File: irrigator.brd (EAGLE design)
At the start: 79.7 x 47 mm, 27 parts, among them IC1 MEGA8-AI, IC2 78L05Z, T1 BT136, X1 MSTBA2

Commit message: fix. errors and manual routing
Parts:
- C3: device rcl:C102-054X133 -> rcl:C1206
- moved L1 55.6 mm to (12.6, 18.4), turned to 180 degrees
- moved C3 54.1 mm to (57.5, 33.6), turned to 180 degrees
- moved R8 50.1 mm to (51.2, 29.4), turned to 270 degrees
- moved R7 48.7 mm to (52.0, 33.6), turned to 180 degrees
- moved C4 46.3 mm to (5.70, 20.9)
- moved C1 46.0 mm to (11.2, 36.2), turned to 180 degrees
- moved JP3 44.6 mm to (5.35, 8.22), turned to 270 degrees
- moved T1 41.4 mm to (59.6, 15.6), turned to 270 degrees
- moved LED1 36.5 mm to (35.8, 20.6)
- moved C2 35.3 mm to (20.7, 37.7)
- moved IC1 33.4 mm to (21.6, 22.4)
- moved LED2 31.6 mm to (35.7, 12.6)
- moved IC2 30.2 mm to (17.6, 32.2), turned to 180 degrees
- moved R5 28.1 mm to (46.0, 12.9), turned to 180 degrees
- moved S2 27.5 mm to (30.4, 4.97), turned to 180 degrees
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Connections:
- new net MISO: IC1.16, JP3.1
- new net MOSI: IC1.15, JP3.4
- new net SCK: IC1.17, JP3.3
- net BUTTON_1: now also IC1.13; no longer IC1.12
- net BUTTON_2: now also IC1.12; no longer IC1.13
- net LED_1: now also IC1.9; no longer IC1.15, JP3.4
- net LED_2: now also IC1.10; no longer IC1.16, JP3.1
- net SENS_IN: no longer JP3.3
- net SW: now also IC1.1; no longer IC1.14
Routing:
- net GND: track 0.00 -> 172.2 mm
- net VCC: track 0.00 -> 94.3 mm, vias 0 -> 2
- net RESET: track 0.00 -> 46.2 mm, vias 0 -> 2
- net N$7: track 0.00 -> 44.4 mm
- net N$8: track 0.00 -> 26.8 mm
- net SCK: track 0.00 -> 25.7 mm
- net BUTTON_2: track 0.00 -> 22.7 mm
- net MOSI: track 0.00 -> 20.7 mm
- net N$6: track 0.00 -> 20.4 mm
- net BUTTON_1: track 0.00 -> 20.4 mm
- net MISO: track 0.00 -> 19.3 mm
- net VIN: track 0.00 -> 15.4 mm
- net SENS_IN: track 0.00 -> 13.4 mm
- net LED_2: track 0.00 -> 13.2 mm
- net N$1: track 0.00 -> 12.8 mm
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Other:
- board size 79.7 x 47 mm -> 74.9 x 42.2 mm

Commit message: minor fix.
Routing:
- net N$8: track 26.8 -> 26.3 mm
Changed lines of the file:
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@@
 <wire x1="58.9" y1="33.6" x2="62.66" y2="34" width="0.4064" layer="16"/>
 <wire x1="62.66" y1="34" x2="64.26" y2="33.88" width="0.4064" layer="16"/>
-<wire x1="53.25" y1="18.14" x2="57.45" y2="18.75" width="0.4064" layer="16"/>
-<wire x1="57.45" y1="18.75" x2="63.8" y2="27.3" width="1.6764" layer="16"/>
 <wire x1="63.8" y1="27.3" x2="64.3" y2="33.84" width="1.6764" layer="16"/>
-<wire x1="64.3" y1="33.84" x2="64.26" y2="33.88" width="0" layer="19" extent="1-16"/>
+<wire x1="53.25" y1="18.14" x2="54.64" y2="18.14" width="1.6764" layer="16"/>
+<wire x1="54.64" y1="18.14" x2="63.8" y2="27.3" width="1.6764" layer="16"/>
+<wire x1="64.3" y1="33.84" x2="64.26" y2="33.88" width="0" layer="19" extent="16-16"/>
 </signal>
 <signal name="N$9">

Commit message: board fix
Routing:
- net VCC: track 94.3 -> 128.0 mm
- net RESET: track 46.2 -> 48.4 mm
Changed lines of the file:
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@@
 <wire x1="25.1" y1="31.7" x2="23.498" y2="33.302" width="0.4064" layer="16"/>
 <wire x1="23.498" y1="33.302" x2="23.36" y2="33.302" width="0.4064" layer="16"/>
-<wire x1="19.46" y1="10.008" x2="19.62" y2="9.848" width="0.4064" layer="16"/>
-<wire x1="19.62" y1="9.848" x2="25.1" y2="9.848" width="0.4064" layer="16"/>
-<wire x1="9.1" y1="18.5" x2="11" y2="18.5" width="0.4064" layer="16"/>
-<wire x1="11" y1="18.5" x2="11.1" y2="18.4" width="0.4064" layer="16"/>
-<wire x1="6.62" y1="10.76" x2="6.56" y2="10.76" width="0.4064" layer="16"/>
-<wire x1="6.56" y1="10.76" x2="5.4" y2="9.6" width="0.4064" layer="16"/>
-<wire x1="5.4" y1="9.6" x2="5.4" y2="7" width="0.4064" layer="16"/>
-<wire x1="5.4" y1="7" x2="10.5" y2="7" width="0.4064" layer="16"/>
-<wire x1="10.5" y1="7" x2="12.7" y2="4.8" width="0.4064" layer="16"/>
-<wire x1="12.7" y1="4.8" x2="24.6" y2="4.8" width="0.4064" layer="16"/>
-<wire x1="24.6" y1="4.8" x2="24.6" y2="9.348" width="0.4064" layer="16"/>
-<wire x1="24.6" y1="9.348" x2="25.1" y2="9.848" width="0.4064" layer="16"/>
-<wire x1="8.8" y1="16.8" x2="8.8" y2="17.6" width="0.4064" layer="16"/>
-<wire x1="8.8" y1="17.6" x2="9.1" y2="18.5" width="0.4064" layer="16"/>
-<via x="8.8" y="16.8" extent="1-16" drill="0.8" diameter="1.6764"/>
-<wire x1="8.8" y1="16.8" x2="9" y2="13.8" width="0.4064" layer="1"/>
-<wire x1="9" y1="13.8" x2="9.2" y2="10.9" width="0.4064" layer="1"/>
-<via x="9.2" y="10.9" extent="1-16" drill="0.8" diameter="1.6764"/>
-<wire x1="9.2" y1="10.9" x2="6.76" y2="10.9" width="0.4064" layer="16"/>
-<wire x1="6.76" y1="10.9" x2="6.62" y2="10.76" width="0.4064" layer="16"/>
 <wire x1="25.8926" y1="21.2" x2="27.1" y2="21.2" width="0.4064" layer="16"/>
 <wire x1="27.1" y1="21.2" x2="27.7" y2="21.8" width="0.4064" layer="16"/>
 <wire x1="27.7" y1="21.8" x2="27.7" y2="22.720471875" width="0.4064" layer="16"/>
 <wire x1="27.7" y1="22.720471875" x2="27.59071875" y2="22.829753125" width="0.4064" layer="16"/>
-<wire x1="11" y1="18.5" x2="11.048" y2="25.04" width="0" layer="19" extent="16-16"/>
+<wire x1="6.62" y1="10.76" x2="6.56" y2="10.76" width="0.4064" layer="16"/>
+<wire x1="6.56" y1="10.76" x2="5.3" y2="9.5" width="0.4064" layer="16"/>
+<wire x1="5.3" y1="9.5" x2="5.3" y2="7.2" width="0.4064" layer="16"/>
+<wire x1="5.3" y1="7.2" x2="5.5" y2="7" width="0.4064" layer="16"/>
+<wire x1="5.5" y1="7" x2="7.8" y2="7" width="0.4064" layer="16"/>
+<wire x1="7.8" y1="7" x2="9.9" y2="4.9" width="0.4064" layer="16"/>
+<wire x1="9.9" y1="4.9" x2="25.2" y2="4.9" width="0.4064" layer="16"/>
+<wire x1="25.2" y1="4.9" x2="35" y2="4.9" width="0.4064" layer="16"/>
+<wire x1="35" y1="4.9" x2="35.7" y2="5.9" width="0.4064" layer="16"/>
+<wire x1="35.7" y1="5.9" x2="35.7" y2="21.5" width="0.4064" layer="16"/>
+<wire x1="35.7" y1="21.5" x2="35" y2="22.9" width="0.4064" layer="16"/>
+<wire x1="35" y1="22.9" x2="31.6" y2="22.9" width="0.4064" layer="16"/>
+<wire x1="25.1" y1="9.848" x2="25.1" y2="5" width="0.4064" layer="16"/>
+<wire x1="25.1" y1="5" x2="25.2" y2="4.9" width="0.4064" layer="16"/>
+<wire x1="25.1" y1="9.848" x2="19.62" y2="9.848" width="0.4064" layer="16"/>
+<wire x1="19.62" y1="9.848" x2="19.46" y2="10.008" width="0.4064" layer="16"/>
+<wire x1="11.1" y1="18.4" x2="8.8" y2="18.4" width="0.4064" layer="16"/>
+<wire x1="8.8" y1="18.4" x2="8.3" y2="17.9" width="0.4064" layer="16"/>
+<via x="8.3" y="17.9" extent="1-16" drill="0.8" diameter="1.6764"/>
+<wire x1="8.3" y1="17.9" x2="8.3" y2="11.7" width="0.4064" layer="1"/>
+<wire x1="8.3" y1="11.7" x2="9.8" y2="10.9" width="0.4064" layer="1"/>
+<via x="9.8" y="10.9" extent="1-16" drill="0.8" diameter="1.6764"/>
+<wire x1="9.8" y1="10.9" x2="6.76" y2="10.9" width="0.4064" layer="16"/>
+<wire x1="6.76" y1="10.9" x2="6.62" y2="10.76" width="0.4064" layer="16"/>
 </signal>
 <signal name="BUTTON_2">
@@
 <wire x1="4.08" y1="4.92" x2="6.5" y2="3" width="0.4064" layer="16"/>
 <via x="6.5" y="3" extent="1-16" drill="0.8" diameter="1.6764"/>
-<wire x1="6.5" y1="3" x2="12.6" y2="10.3" width="0.4064" layer="1"/>
-<wire x1="12.6" y1="10.3" x2="20.1" y2="28.7" width="0.4064" layer="1"/>
 <via x="20.1" y="28.7" extent="1-16" drill="0.8" diameter="1.6764"/>
 <wire x1="20.1" y1="28.7" x2="21.7" y2="28.7" width="0.4064" layer="16"/>
 <wire x1="21.7" y1="28.7" x2="22" y2="28.4" width="0.4064" layer="16"/>
+<wire x1="6.5" y1="3" x2="12.8" y2="7.3" width="0.4064" layer="1"/>
+<wire x1="12.8" y1="7.3" x2="12.8" y2="19.4" width="0.4064" layer="1"/>
+<wire x1="12.8" y1="19.4" x2="20.1" y2="28.7" width="0.4064" layer="1"/>
 </signal>
 <signal name="LED_1">

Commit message: brd fix.
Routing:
- net VCC: track 128.0 -> 129.3 mm
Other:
- board size 74.9 x 42.2 mm -> 74.9 x 42.4 mm
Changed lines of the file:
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@@
 <layer number="27" name="tValues" color="7" fill="1" visible="yes" active="yes"/>
 <layer number="28" name="bValues" color="7" fill="1" visible="yes" active="yes"/>
-<layer number="29" name="tStop" color="7" fill="3" visible="no" active="yes"/>
-<layer number="30" name="bStop" color="7" fill="6" visible="no" active="yes"/>
-<layer number="31" name="tCream" color="7" fill="4" visible="no" active="yes"/>
-<layer number="32" name="bCream" color="7" fill="5" visible="no" active="yes"/>
-<layer number="33" name="tFinish" color="6" fill="3" visible="no" active="yes"/>
-<layer number="34" name="bFinish" color="6" fill="6" visible="no" active="yes"/>
-<layer number="35" name="tGlue" color="7" fill="4" visible="no" active="yes"/>
-<layer number="36" name="bGlue" color="7" fill="5" visible="no" active="yes"/>
-<layer number="37" name="tTest" color="7" fill="1" visible="no" active="yes"/>
-<layer number="38" name="bTest" color="7" fill="1" visible="no" active="yes"/>
+<layer number="29" name="tStop" color="7" fill="3" visible="yes" active="yes"/>
+<layer number="30" name="bStop" color="7" fill="6" visible="yes" active="yes"/>
+<layer number="31" name="tCream" color="7" fill="4" visible="yes" active="yes"/>
+<layer number="32" name="bCream" color="7" fill="5" visible="yes" active="yes"/>
+<layer number="33" name="tFinish" color="6" fill="3" visible="yes" active="yes"/>
+<layer number="34" name="bFinish" color="6" fill="6" visible="yes" active="yes"/>
+<layer number="35" name="tGlue" color="7" fill="4" visible="yes" active="yes"/>
+<layer number="36" name="bGlue" color="7" fill="5" visible="yes" active="yes"/>
+<layer number="37" name="tTest" color="7" fill="1" visible="yes" active="yes"/>
+<layer number="38" name="bTest" color="7" fill="1" visible="yes" active="yes"/>
 <layer number="39" name="tKeepout" color="4" fill="11" visible="yes" active="yes"/>
 <layer number="40" name="bKeepout" color="1" fill="11" visible="yes" active="yes"/>
@@
 <layer number="42" name="bRestrict" color="1" fill="10" visible="yes" active="yes"/>
 <layer number="43" name="vRestrict" color="2" fill="10" visible="yes" active="yes"/>
-<layer number="44" name="Drills" color="7" fill="1" visible="no" active="yes"/>
-<layer number="45" name="Holes" color="7" fill="1" visible="no" active="yes"/>
-<layer number="46" name="Milling" color="3" fill="1" visible="no" active="yes"/>
-<layer number="47" name="Measures" color="7" fill="1" visible="no" active="yes"/>
+<layer number="44" name="Drills" color="7" fill="1" visible="yes" active="yes"/>
+<layer number="45" name="Holes" color="7" fill="1" visible="yes" active="yes"/>
+<layer number="46" name="Milling" color="3" fill="1" visible="yes" active="yes"/>
+<layer number="47" name="Measures" color="7" fill="1" visible="yes" active="yes"/>
 <layer number="48" name="Document" color="7" fill="1" visible="yes" active="yes"/>
 <layer number="49" name="Reference" color="7" fill="1" visible="yes" active="yes"/>
@@
 <plain>
 <wire x1="0" y1="0" x2="74.88" y2="0.1" width="0" layer="20"/>
-<wire x1="74.88" y1="0.1" x2="74.78" y2="42.18" width="0" layer="20"/>
-<wire x1="74.78" y1="42.18" x2="0" y2="42.18" width="0" layer="20"/>
+<wire x1="74.88" y1="0.1" x2="74.88" y2="42.38" width="0" layer="20"/>
+<wire x1="74.88" y1="42.38" x2="0" y2="42.18" width="0" layer="20"/>
 <wire x1="0" y1="42.18" x2="0" y2="0" width="0" layer="20"/>
 </plain>
@@
 <wire x1="9.9" y1="4.9" x2="25.2" y2="4.9" width="0.4064" layer="16"/>
 <wire x1="25.2" y1="4.9" x2="35" y2="4.9" width="0.4064" layer="16"/>
-<wire x1="35" y1="4.9" x2="35.7" y2="5.9" width="0.4064" layer="16"/>
-<wire x1="35.7" y1="5.9" x2="35.7" y2="21.5" width="0.4064" layer="16"/>
-<wire x1="35.7" y1="21.5" x2="35" y2="22.9" width="0.4064" layer="16"/>
-<wire x1="35" y1="22.9" x2="31.6" y2="22.9" width="0.4064" layer="16"/>
+<wire x1="35.8" y1="21.5" x2="35.1" y2="22.9" width="0.4064" layer="16"/>
+<wire x1="35.1" y1="22.9" x2="31.6" y2="22.9" width="0.4064" layer="16"/>
 <wire x1="25.1" y1="9.848" x2="25.1" y2="5" width="0.4064" layer="16"/>
 <wire x1="25.1" y1="5" x2="25.2" y2="4.9" width="0.4064" layer="16"/>
@@
 <wire x1="9.8" y1="10.9" x2="6.76" y2="10.9" width="0.4064" layer="16"/>
 <wire x1="6.76" y1="10.9" x2="6.62" y2="10.76" width="0.4064" layer="16"/>
+<wire x1="35.8" y1="21.6" x2="35.8" y2="21.5" width="0.4064" layer="16"/>
+<wire x1="35.8" y1="21.5" x2="35.8" y2="9.2" width="0.4064" layer="16"/>
+<wire x1="35.8" y1="9.2" x2="37.1" y2="7.6" width="0.4064" layer="16"/>
+<wire x1="37.1" y1="7.6" x2="37.1" y2="7" width="0.4064" layer="16"/>
+<wire x1="37.1" y1="7" x2="35" y2="4.9" width="0.4064" layer="16"/>
 </signal>
 <signal name="BUTTON_2">
@@
 <contactref element="OK1" pad="1"/>
 <wire x1="33.022" y1="25.4" x2="35.3" y2="25.4" width="0.4064" layer="16"/>
-<wire x1="35.3" y1="25.4" x2="36.5" y2="26.6" width="0.4064" layer="16"/>
-<wire x1="36.5" y1="26.6" x2="36.5" y2="32.1" width="0.4064" layer="16"/>
-<wire x1="36.5" y1="32.1" x2="38.04" y2="33.64" width="0.4064" layer="16"/>
+<wire x1="35.3" y1="25.4" x2="36.4" y2="26.6" width="0.4064" layer="16"/>
+<wire x1="36.4" y1="26.6" x2="36.4" y2="32.1" width="0.4064" layer="16"/>
+<wire x1="36.4" y1="32.1" x2="38.04" y2="33.64" width="0.4064" layer="16"/>
 <wire x1="38.04" y1="33.64" x2="39.19" y2="33.64" width="0.4064" layer="16"/>
 </signal>

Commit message: fix. and topor files
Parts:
- moved C4 0.36 mm to (5.50, 20.6)
- moved JP2 0.30 mm to (5.19, 26.0)
- moved R5 0.10 mm to (46.0, 12.9)
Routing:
- net N$7: track 44.4 -> 46.1 mm
- net GND: track 172.2 -> 173.4 mm
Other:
- board size 74.9 x 42.4 mm -> 74.9 x 42.2 mm

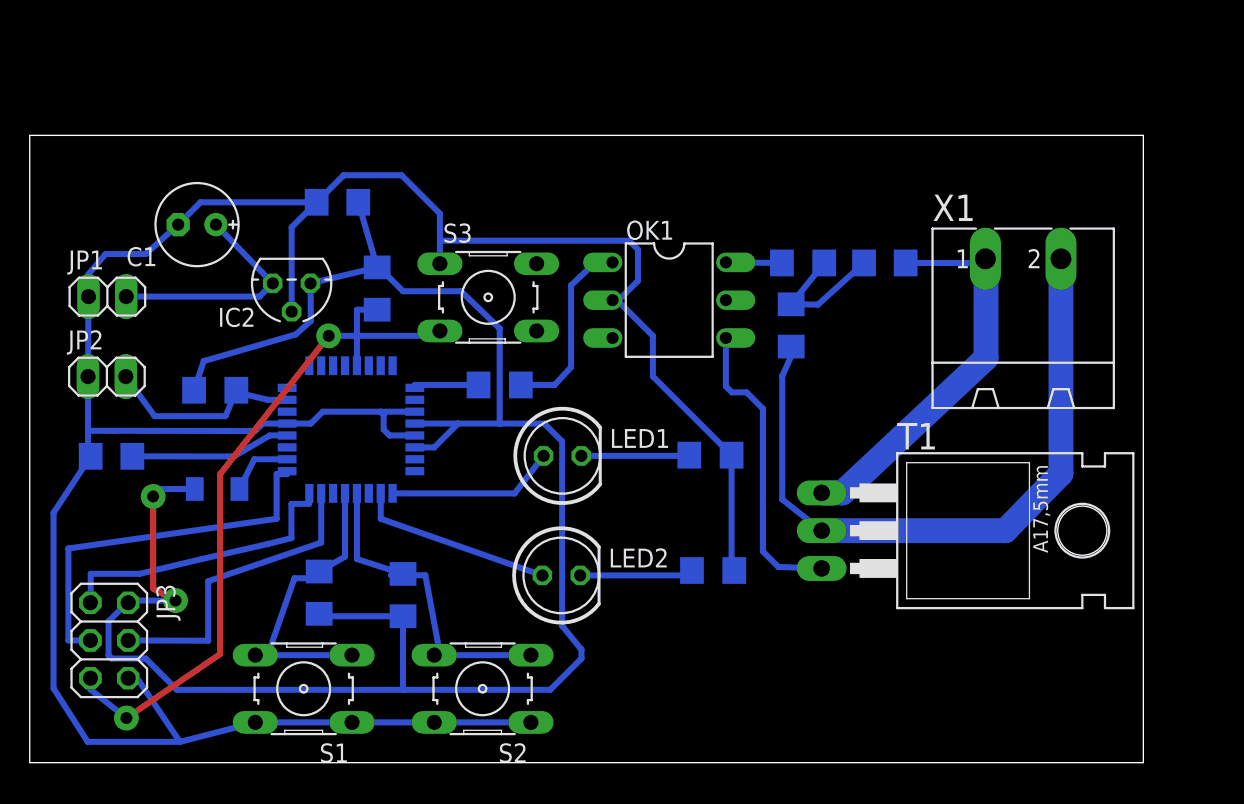
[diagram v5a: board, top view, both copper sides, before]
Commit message: add sensor switch
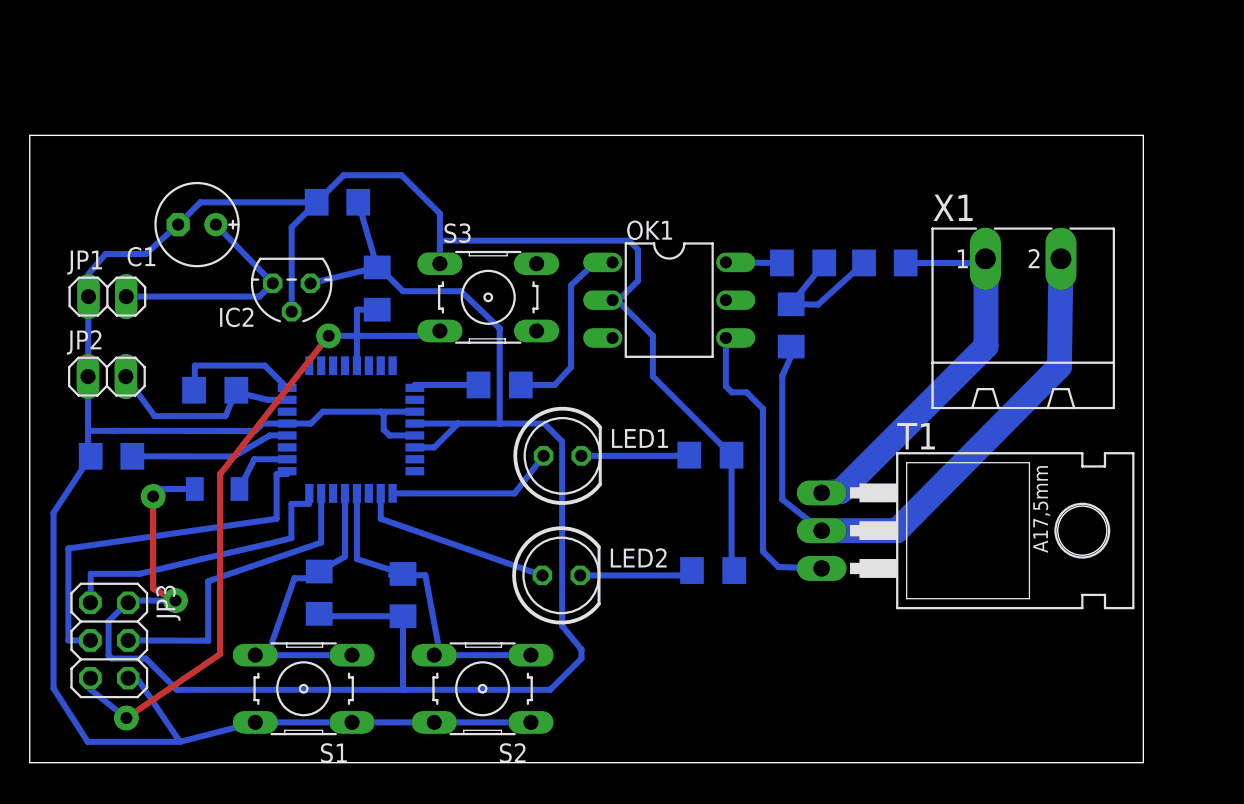
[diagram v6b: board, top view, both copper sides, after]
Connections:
- new net SENS_SW: IC1.24, R1.2
- net VCC: no longer R1.2
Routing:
- net VCC: track 129.5 -> 117.1 mm
- net SENS_SW: track 0.00 -> 8.54 mm
- net N$7: track 46.1 -> 41.7 mm
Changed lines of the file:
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@@
 <?xml version="1.0" encoding="utf-8"?>
 <!DOCTYPE eagle SYSTEM "eagle.dtd">
-<eagle version="7.7.0">
+<eagle version="8.0.0">
 <drawing>
 <settings>
@@
 <contactref element="C2" pad="1"/>
 <contactref element="IC2" pad="1"/>
-<contactref element="R1" pad="2"/>
 <contactref element="R2" pad="1"/>
 <contactref element="R3" pad="1"/>
@@
 <wire x1="18.88" y1="32.23" x2="23.36" y2="33.302" width="0.4064" layer="16"/>
 <wire x1="23.36" y1="33.302" x2="22.09" y2="37.68" width="0.4064" layer="16"/>
-<wire x1="18.88" y1="32.23" x2="18.9" y2="29.7" width="0.4064" layer="16"/>
-<wire x1="18.9" y1="29.7" x2="17.9" y2="28.8" width="0.4064" layer="16"/>
-<wire x1="17.9" y1="28.8" x2="11.7" y2="27" width="0.4064" layer="16"/>
-<wire x1="11.7" y1="27" x2="11.048" y2="25.04" width="0.4064" layer="16"/>
 <wire x1="31.6" y1="29.2" x2="29" y2="31.7" width="0.4064" layer="16"/>
 <wire x1="29" y1="31.7" x2="25.1" y2="31.7" width="0.4064" layer="16"/>
@@
 <wire x1="50.6" y1="26" x2="51.4" y2="27.778" width="0.4064" layer="16"/>
 <wire x1="51.4" y1="27.778" x2="51.2" y2="27.978" width="0.4064" layer="16"/>
-<wire x1="69.34" y1="33.88" x2="69.34" y2="19.44" width="1.6764" layer="16"/>
-<wire x1="69.34" y1="19.44" x2="65.6" y2="15.6" width="1.6764" layer="16"/>
-<wire x1="65.6" y1="15.6" x2="53.25" y2="15.6" width="1.6764" layer="16"/>
+<wire x1="69.34" y1="33.88" x2="69.24" y2="26.64" width="1.6764" layer="16"/>
+<wire x1="69.24" y1="26.64" x2="58.3" y2="15.6" width="1.6764" layer="16"/>
+<wire x1="58.3" y1="15.6" x2="53.25" y2="15.6" width="1.6764" layer="16"/>
 </signal>
 <signal name="N$6">
@@
 <wire x1="58.9" y1="33.6" x2="63.76" y2="33.6" width="0.4064" layer="16"/>
 <wire x1="63.76" y1="33.6" x2="64.26" y2="33.88" width="0.4064" layer="16"/>
-<wire x1="64.3" y1="27.2" x2="64.3" y2="33.84" width="1.6764" layer="16"/>
-<wire x1="53.25" y1="18.14" x2="54.64" y2="18.14" width="1.6764" layer="16"/>
-<wire x1="54.64" y1="18.14" x2="64.3" y2="27.2" width="1.6764" layer="16"/>
+<wire x1="64.3" y1="28" x2="64.3" y2="33.84" width="1.6764" layer="16"/>
+<wire x1="53.25" y1="18.14" x2="54.54" y2="18.24" width="1.6764" layer="16"/>
+<wire x1="54.54" y1="18.24" x2="64.3" y2="28" width="1.6764" layer="16"/>
 <wire x1="64.3" y1="33.84" x2="64.26" y2="33.88" width="0" layer="19" extent="16-16"/>
 </signal>
@@
 <signal name="N$12">
 </signal>
+<signal name="SENS_SW">
+<contactref element="R1" pad="2"/>
+<contactref element="IC1" pad="24"/>
+<wire x1="11.048" y1="25.04" x2="11.1" y2="25.04" width="0.4064" layer="16"/>
+<wire x1="11.1" y1="25.04" x2="11.1" y2="26.7" width="0.4064" layer="16"/>
+<wire x1="11.1" y1="26.7" x2="15.8074" y2="26.7" width="0.4064" layer="16"/>
+<wire x1="15.8074" y1="26.7" x2="17.3074" y2="25.2" width="0.4064" layer="16"/>
+</signal>
 </signals>
